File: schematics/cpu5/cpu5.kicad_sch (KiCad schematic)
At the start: 9 parts, among them J1 Conn_01x12, U1 74LS161, U2 74LS161, U3 74LS573, U4 74LS04, U5 74LS08, U6 74LS32, U7 74LS08

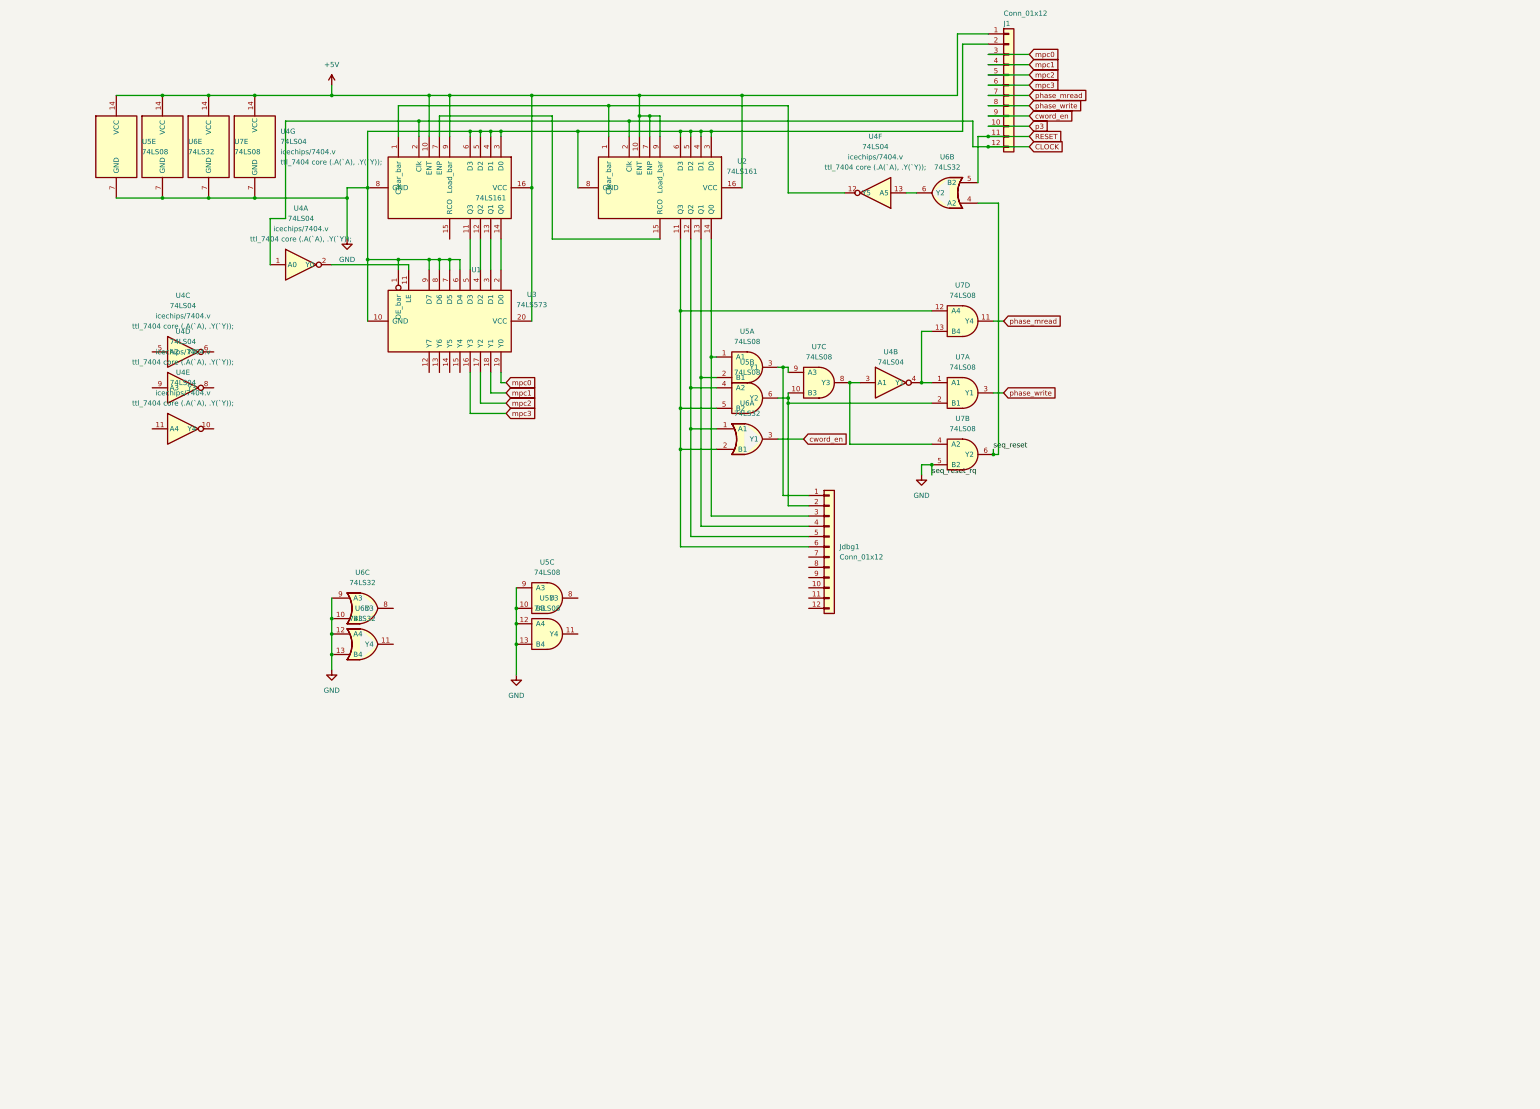
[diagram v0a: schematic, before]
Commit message: microcode rom works
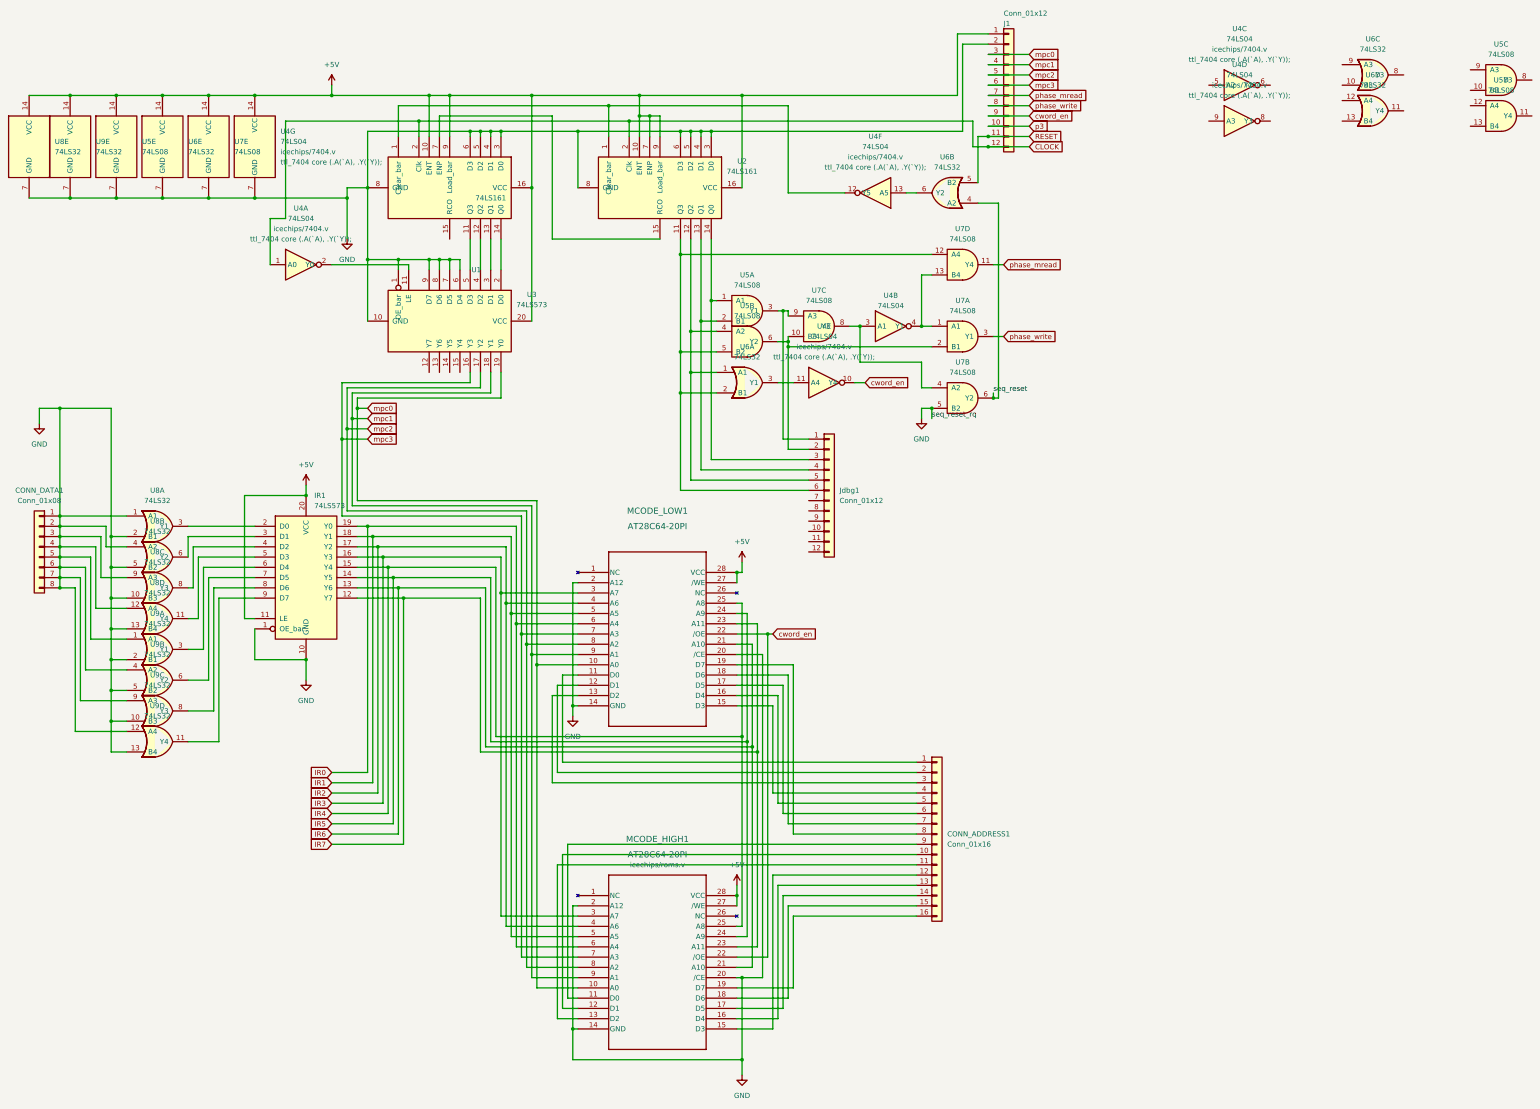
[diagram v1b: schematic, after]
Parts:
- added CONN_ADDRESS1: Conn_01x16, Connector_PinHeader_2.54mm:PinHeader_1x16_P2.54mm_Vertical, symbol Connector_Generic:Conn_01x16
- added CONN_DATA1: Conn_01x08, Connector_PinHeader_2.54mm:PinHeader_1x08_P2.54mm_Vertical, symbol Connector_Generic:Conn_01x08
- added IR1: 74LS573, Package_DIP:DIP-20_W7.62mm, symbol 7400_ice:74LS573
- added MCODE_HIGH1, MCODE_LOW1: AT28C64-20PI, Package_DIP:DIP-28_W15.24mm, symbol at28c64:AT28C64-20PI
- added U8, U9: 74LS32, Package_DIP:DIP-14_W7.62mm, symbol 7400_ice:74LS32
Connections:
- net +5V: now also IR1.11 (LE), IR1.20 (VCC), MCODE_HIGH1.27 (/WE), MCODE_HIGH1.28 (VCC), MCODE_LOW1.27 (/WE), MCODE_LOW1.28 (VCC), U8.14 (VCC), U9.14 (VCC)
- net GND: now also CONN_DATA1.1 (Pin_1), CONN_DATA1.2 (Pin_2), CONN_DATA1.3 (Pin_3), CONN_DATA1.4 (Pin_4), CONN_DATA1.5 (Pin_5), CONN_DATA1.6 (Pin_6), CONN_DATA1.7 (Pin_7), CONN_DATA1.8 (Pin_8), IR1.1 (OE_bar), IR1.10 (GND), MCODE_HIGH1.14 (GND), MCODE_HIGH1.2 (A12), MCODE_HIGH1.20 (/CE), MCODE_LOW1.14 (GND), MCODE_LOW1.2 (A12), MCODE_LOW1.20 (/CE), U8.1 (A1), U8.10 (B3), U8.12 (A4), U8.13 (B4), U8.2 (B1), U8.4 (A2), U8.5 (B2), U8.7 (GND), U8.9 (A3), U9.1 (A1), U9.10 (B3), U9.12 (A4), U9.13 (B4), U9.2 (B1), U9.4 (A2), U9.5 (B2), U9.7 (GND), U9.9 (A3); no longer U5.10 (B3), U5.12 (A4), U5.13 (B4), U5.9 (A3), U6.10 (B3), U6.12 (A4), U6.13 (B4), U6.9 (A3)
- net cword_en: now also U4.10 (Y4), MCODE_HIGH1.22 (/OE), MCODE_LOW1.22 (/OE); no longer U6.3 (Y1)
- net mpc0: now also MCODE_HIGH1.10 (A0), MCODE_LOW1.10 (A0)
- net mpc1: now also MCODE_HIGH1.9 (A1), MCODE_LOW1.9 (A1)
- net mpc2: now also MCODE_HIGH1.8 (A2), MCODE_LOW1.8 (A2)
- net mpc3: now also MCODE_HIGH1.7 (A3), MCODE_LOW1.7 (A3)
- net at U4.11 (A4): now also U6.3 (Y1)
- new net: IR1.7 (D5), U9.6 (Y2)
- new net: IR1.9 (D7), U9.11 (Y4)
- new net: IR1.2 (D0), U8.3 (Y1)
- new net: IR1.4 (D2), U8.8 (Y3)
- new net: IR1.5 (D3), U8.11 (Y4)
- new net: CONN_ADDRESS1.1 (Pin_1), MCODE_LOW1.11 (D0)
- new net: CONN_ADDRESS1.10 (Pin_10), MCODE_HIGH1.12 (D1)
- new net: CONN_ADDRESS1.11 (Pin_11), MCODE_HIGH1.13 (D2)
- new net: CONN_ADDRESS1.12 (Pin_12), MCODE_HIGH1.15 (D3)
- new net: CONN_ADDRESS1.13 (Pin_13), MCODE_HIGH1.16 (D4)
- new net: CONN_ADDRESS1.14 (Pin_14), MCODE_HIGH1.17 (D5)
- new net: CONN_ADDRESS1.15 (Pin_15), MCODE_HIGH1.18 (D6)
- new net: CONN_ADDRESS1.16 (Pin_16), MCODE_HIGH1.19 (D7)
- new net: CONN_ADDRESS1.2 (Pin_2), MCODE_LOW1.12 (D1)
- new net: CONN_ADDRESS1.3 (Pin_3), MCODE_LOW1.13 (D2)
- new net: CONN_ADDRESS1.4 (Pin_4), MCODE_LOW1.15 (D3)
- new net: CONN_ADDRESS1.5 (Pin_5), MCODE_LOW1.16 (D4)
- new net: CONN_ADDRESS1.6 (Pin_6), MCODE_LOW1.17 (D5)
- new net: CONN_ADDRESS1.7 (Pin_7), MCODE_LOW1.18 (D6)
- new net: CONN_ADDRESS1.8 (Pin_8), MCODE_LOW1.19 (D7)
- new net: CONN_ADDRESS1.9 (Pin_9), MCODE_HIGH1.11 (D0)
- new net: IR1.6 (D4), U9.3 (Y1)
- new net: IR1.3 (D1), U8.6 (Y2)
- new net: IR1.8 (D6), U9.8 (Y3)
- new net IR0: IR1.19 (Y0), MCODE_HIGH1.6 (A4), MCODE_LOW1.6 (A4)
- new net IR1: IR1.18 (Y1), MCODE_HIGH1.5 (A5), MCODE_LOW1.5 (A5)
- new net IR2: IR1.17 (Y2), MCODE_HIGH1.4 (A6), MCODE_LOW1.4 (A6)
- new net IR3: IR1.16 (Y3), MCODE_HIGH1.3 (A7), MCODE_LOW1.3 (A7)
- new net IR4: IR1.15 (Y4), MCODE_HIGH1.25 (A8), MCODE_LOW1.25 (A8)
- new net IR5: IR1.14 (Y5), MCODE_HIGH1.24 (A9), MCODE_LOW1.24 (A9)
- new net IR6: IR1.13 (Y6), MCODE_HIGH1.21 (A10), MCODE_LOW1.21 (A10)
- new net IR7: IR1.12 (Y7), MCODE_HIGH1.23 (A11), MCODE_LOW1.23 (A11)
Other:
- moved on the sheet: Jdbg1, U4B, U4C, U4D, U4E, U5A, U5B, U5C, U5D, U6A, U6C, U6D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

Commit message: nop works
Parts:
- removed IR1, U3: 74LS573, Package_DIP:DIP-20_W7.62mm, symbol 7400_ice:74LS573
- added IR1, U10, U11: 74LS574, Package_DIP:DIP-20_W7.62mm, symbol 7400_ice:74LS574
- added J2: Conn_01x03, Connector_PinHeader_2.54mm:PinHeader_1x03_P2.54mm_Vertical, symbol Connector_Generic:Conn_01x03
- added J3: Conn_01x40, Connector_PinHeader_2.54mm:PinHeader_1x40_P2.54mm_Vertical, symbol Connector_Generic:Conn_01x40
- added JFlags1: Conn_01x04, Connector_PinHeader_1.00mm:PinHeader_1x04_P1.00mm_Vertical, symbol Connector_Generic:Conn_01x04
- added U12, U21, U26, U31: 74LS08, Package_DIP:DIP-14_W7.62mm, symbol 7400_ice:74LS08
- added U13, U14, U15, U16, U17, U18, U19, U20, U27: 74LS138, Package_DIP:DIP-16_W7.62mm, symbol 7400_ice:74LS138
- added U22, U28: 74LS04, Package_DIP:DIP-14_W7.62mm, symbol 7400_ice:74LS04
- added U23, U25: 74LS86, Package_DIP:DIP-14_W7.62mm, symbol 7400_ice:74LS86
- added U24, U29, U30, U32, U33: 74LS32, Package_DIP:DIP-14_W7.62mm, symbol 7400_ice:74LS32
- added U34: 74LS74, Package_DIP:DIP-14_W7.62mm, symbol 7400_ice:74LS74
- added U35, U36, U42: 74LS541, Package_DIP:DIP-20_W7.62mm, symbol 7400_ice:74LS541
- CONN_DATA1: VerilogModulePort (none) -> 1,2,3,4,5,6,7,8
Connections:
- net +5V: now also IR1.20 (VCC), U10.20 (VCC), U11.20 (VCC), U12.14 (VCC), U13.16 (VCC), U14.16 (VCC), U15.16 (VCC), U16.16 (VCC), U17.16 (VCC), U18.16 (VCC), U19.16 (VCC), U20.16 (VCC), U21.14 (VCC), U22.14 (VCC), U23.14 (VCC), U24.14 (VCC), U25.14 (VCC), U26.14 (VCC), U27.16 (VCC), U27.6 (Enable3), U28.14 (VCC), U29.14 (VCC), U30.14 (VCC), U31.14 (VCC), U32.14 (VCC), U33.14 (VCC), U34.14 (VCC), U34.4 (nS1), U35.20 (VCC), U35.8 (A6), U35.9 (A7), U36.20 (VCC), U36.4 (A2), U36.5 (A3), U36.6 (A4), U36.7 (A5), U36.9 (A7), U42.2 (A0), U42.20 (VCC), U42.3 (A1), U42.4 (A2), U42.5 (A3), U42.6 (A4), U42.7 (A5), U42.8 (A6), U42.9 (A7); no longer U1.9 (Load_bar), U2.9 (Load_bar)
- net CLOCK: now also U26.13 (B4); no longer U4.1 (A0)
- net GND: now also MCODE_HIGH1.22 (/OE), MCODE_LOW1.22 (/OE), IR1.1 (OE_bar), IR1.10 (GND), U10.1 (OE_bar), U10.10 (GND), U11.1 (OE_bar), U11.10 (GND), U12.7 (GND), U13.4 (Enable1_bar), U13.8 (GND), U14.4 (Enable1_bar), U14.8 (GND), U15.4 (Enable1_bar), U15.8 (GND), U16.4 (Enable1_bar), U16.8 (GND), U17.4 (Enable1_bar), U17.8 (GND), U18.4 (Enable1_bar), U18.8 (GND), U19.4 (Enable1_bar), U19.8 (GND), U20.4 (Enable1_bar), U20.8 (GND), U21.7 (GND), U22.7 (GND), U23.7 (GND), U24.7 (GND), U25.7 (GND), U26.7 (GND), U27.4 (Enable1_bar), U27.5 (Enable2_bar), U27.8 (GND), U28.7 (GND), U29.7 (GND), U30.7 (GND), U31.7 (GND), U32.7 (GND), U33.7 (GND), U34.7 (GND), U35.1 (OE1_bar), U35.10 (GND), U35.7 (A5), U36.1 (OE1_bar), U36.10 (GND), U36.8 (A6), U42.10 (GND), U42.19 (OE2_bar); no longer CONN_DATA1.1 (Pin_1), CONN_DATA1.2 (Pin_2), CONN_DATA1.3 (Pin_3), CONN_DATA1.4 (Pin_4), CONN_DATA1.5 (Pin_5), CONN_DATA1.6 (Pin_6), CONN_DATA1.7 (Pin_7), CONN_DATA1.8 (Pin_8), U7.5 (B2), U8.1 (A1), U8.12 (A4), U8.4 (A2), U8.9 (A3), U9.1 (A1), U9.12 (A4), U9.4 (A2), U9.9 (A3)
- net IR0: now also IR1.19 (Y0), U27.1 (A0), U35.2 (A0)
- net IR1: now also IR1.18 (Y1), U27.2 (A1), U35.3 (A1)
- net IR2: now also IR1.17 (Y2), U27.3 (A2), U35.4 (A2)
- net IR3: now also IR1.16 (Y3), U23.12 (A4), U23.4 (A2), U23.9 (A3), U25.1 (A1), U25.4 (A2), U35.5 (A3)
- net IR4: now also IR1.15 (Y4), U35.6 (A4)
- net IR5: now also IR1.14 (Y5)
- net IR6: now also IR1.13 (Y6)
- net IR7: now also IR1.12 (Y7)
- net RESET: now also U1.1 (Clear_bar), U2.1 (Clear_bar), U28.3 (A1), U34.1 (nR1); no longer U6.5 (B2)
- net cword_en: now also U5.8 (Y3), U10.11 (CLK), U11.11 (CLK); no longer MCODE_HIGH1.22 (/OE), MCODE_LOW1.22 (/OE), U4.10 (Y4)
- net mpc0: now also U1.14 (Q0)
- net mpc1: now also U1.13 (Q1)
- net mpc2: now also U1.12 (Q2)
- net mpc3: now also U1.11 (Q3)
- net phase_mread: now also U21.5 (B2)
- net phase_write: now also U12.10 (B3), U12.13 (B4), U12.2 (B1), U12.5 (B2), U21.10 (B3), U21.2 (B1)
- net seq_reset: now also U4.13 (A5), U24.12 (A4); no longer U6.4 (A2)
- net at Jdbg1.3 (Pin_3), U2.14 (Q0), U5.1 (A1): now also U5.9 (A3)
- net at Jdbg1.5 (Pin_5), U2.12 (Q2), U5.4 (A2): now also U5.10 (B3); no longer U6.1 (A1)
- net at Jdbg1.6 (Pin_6), U2.11 (Q3), U5.5 (B2)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: no longer U6.2 (B1)
- net iIR5: now reaches U9.6 (Y2)
- net iIR5: now also IR1.7 (D5)
- net at U4.11 (A4): now also U33.11 (Y4); no longer U6.3 (Y1)
- net iIR7: now reaches U9.11 (Y4)
- net iIR7: now also IR1.9 (D7)
- net iIR0: now reaches U8.3 (Y1)
- net iIR0: now also IR1.2 (D0)
- net iIR2: now reaches U8.8 (Y3)
- net iIR2: now also IR1.4 (D2)
- net at U5.11 (Y4): now also U26.4 (A2)
- net at U5.12 (A4): now also U6.6 (Y2)
- net at U5.13 (B4): now also U6.3 (Y1)
- net iIR3: now reaches U8.11 (Y4)
- net iIR3: now also IR1.5 (D3)
- net at U6.10 (B3): now also U23.11 (Y4)
- net at U6.8 (Y3): now also U21.12 (A4)
- net at U6.9 (A3): now also U27.13 (Y2)
- net at U6.11 (Y4): now also U21.13 (B4)
- net at U6.12 (A4): now also U27.12 (Y3)
- net at U6.13 (B4): now also U25.3 (Y1)
- net at CONN_ADDRESS1.1 (Pin_1): now also U35.18 (Y0), U36.18 (Y0); no longer MCODE_LOW1.11 (D0)
- net at CONN_ADDRESS1.10 (Pin_10): now also U42.17 (Y1); no longer MCODE_HIGH1.12 (D1)
- net at CONN_ADDRESS1.11 (Pin_11): now also U42.16 (Y2); no longer MCODE_HIGH1.13 (D2)
- net at CONN_ADDRESS1.12 (Pin_12): now also U42.15 (Y3); no longer MCODE_HIGH1.15 (D3)
- net at CONN_ADDRESS1.13 (Pin_13): now also U42.14 (Y4); no longer MCODE_HIGH1.16 (D4)
- net at CONN_ADDRESS1.14 (Pin_14): now also U42.13 (Y5); no longer MCODE_HIGH1.17 (D5)
- net at CONN_ADDRESS1.15 (Pin_15): now also U42.12 (Y6); no longer MCODE_HIGH1.18 (D6)
- net at CONN_ADDRESS1.16 (Pin_16): now also U42.11 (Y7); no longer MCODE_HIGH1.19 (D7)
- net at CONN_ADDRESS1.2 (Pin_2): now also U35.17 (Y1), U36.17 (Y1); no longer MCODE_LOW1.12 (D1)
- net at CONN_ADDRESS1.3 (Pin_3): now also U35.16 (Y2), U36.16 (Y2); no longer MCODE_LOW1.13 (D2)
- net at CONN_ADDRESS1.4 (Pin_4): now also U35.15 (Y3), U36.15 (Y3); no longer MCODE_LOW1.15 (D3)
- net at CONN_ADDRESS1.5 (Pin_5): now also U35.14 (Y4), U36.14 (Y4); no longer MCODE_LOW1.16 (D4)
- net at CONN_ADDRESS1.6 (Pin_6): now also U35.13 (Y5), U36.13 (Y5); no longer MCODE_LOW1.17 (D5)
- net at CONN_ADDRESS1.7 (Pin_7): now also U35.12 (Y6), U36.12 (Y6); no longer MCODE_LOW1.18 (D6)
- net at CONN_ADDRESS1.8 (Pin_8): now also U35.11 (Y7), U36.11 (Y7); no longer MCODE_LOW1.19 (D7)
- net at CONN_ADDRESS1.9 (Pin_9): now also U42.18 (Y0); no longer MCODE_HIGH1.11 (D0)
- net iIR4: now reaches U9.3 (Y1)
- net iIR4: now also IR1.6 (D4)
- net at U4.5 (A2): now also U13.10 (Y5)
- net at U4.6 (Y2): now also U24.13 (B4)
- net at U4.8 (Y3): now also U17.5 (Enable2_bar), U18.5 (Enable2_bar), U19.5 (Enable2_bar), U20.5 (Enable2_bar)
- net dbg_mcode15: now reaches U4.9 (A3)
- net dbg_mcode15: now also U11.12 (Y7), U13.5 (Enable2_bar), U14.5 (Enable2_bar), U15.5 (Enable2_bar), U16.5 (Enable2_bar)
- net iIR1: now reaches U8.6 (Y2)
- net iIR1: now also IR1.3 (D1)
- net iIR6: now reaches U9.8 (Y3)
- net iIR6: now also IR1.8 (D6)
- new net: U12.11 (Y4), U20.6 (Enable3)
- new net: U15.15 (Y0), U22.5 (A2)
- new net: U12.6 (Y2), U16.6 (Enable3)
- new net: U21.6 (Y2), U22.11 (A4)
- new net: U30.8 (Y3), U31.2 (B1)
- new net: U14.7 (Y7), U30.9 (A3), U33.4 (A2)
- new net: U21.8 (Y3), U22.13 (A5)
- new net: U34.3 (Clk1), U4.10 (Y4)
- new net: U16.12 (Y3), U22.1 (A0)
- new net: U13.7 (Y7), U29.4 (A2), U32.1 (A1)
- new net: U27.14 (Y1), U6.1 (A1)
- new net: U23.8 (Y3), U6.2 (B1)
- new net: MCODE_HIGH1.11 (D0), U11.2 (D0)
- new net: MCODE_HIGH1.12 (D1), U11.3 (D1)
- new net: MCODE_HIGH1.13 (D2), U11.4 (D2)
- new net: MCODE_HIGH1.15 (D3), U11.5 (D3)
- new net: MCODE_HIGH1.16 (D4), U11.6 (D4)
- new net: MCODE_HIGH1.17 (D5), U11.7 (D5)
- new net: MCODE_HIGH1.18 (D6), U11.8 (D6)
- new net: MCODE_HIGH1.19 (D7), U11.9 (D7)
- new net: U15.9 (Y6), U29.9 (A3), U32.4 (A2)
- new net: U16.9 (Y6), U30.1 (A1), U32.12 (A4)
- new net: U1.9 (Load_bar), U2.9 (Load_bar), U4.12 (Y5)
- new net: U16.15 (Y0), U28.11 (A4)
- new net: U16.7 (Y7), U33.12 (A4)
- new net: U31.11 (Y4), U42.1 (OE1_bar)
- new net: U28.6 (Y2), U31.12 (A4), U36.19 (OE2_bar)
- new net: U23.6 (Y2), U6.5 (B2)
- new net: U29.10 (B3), U29.12 (A4), U29.2 (B1), U29.5 (B2), U30.2 (B1), U30.5 (B2), U33.5 (B2), U34.2 (D1), U34.6 (nQ1)
- new net: U26.12 (A4), U28.4 (Y1)
- new net: U23.13 (B4), U24.6 (Y2)
- new net: U12.3 (Y1), U15.6 (Enable3)
- new net: U23.3 (Y1), U24.4 (A2), U25.5 (B2)
- new net: U24.1 (A1), U27.11 (Y4)
- new net: U24.2 (B1), U25.6 (Y2)
- new net: U24.3 (Y1), U26.1 (A1)
- new net: U27.15 (Y0), U6.4 (A2)
- new net: U30.6 (Y2), U31.1 (A1)
- new net: U15.12 (Y3), U22.3 (A1)
- new net: U16.11 (Y4), U28.13 (A5)
- new net: IR1.11 (CLK), U32.8 (Y3)
- new net: MCODE_LOW1.11 (D0), U10.2 (D0)
- new net: MCODE_LOW1.12 (D1), U10.3 (D1)
- new net: MCODE_LOW1.13 (D2), U10.4 (D2)
- new net: MCODE_LOW1.15 (D3), U10.5 (D3)
- new net: MCODE_LOW1.16 (D4), U10.6 (D4)
- new net: MCODE_LOW1.17 (D5), U10.7 (D5)
- new net: MCODE_LOW1.18 (D6), U10.8 (D6)
- new net: MCODE_LOW1.19 (D7), U10.9 (D7)
- new net: U12.8 (Y3), U19.6 (Enable3)
- new net: U24.8 (Y3), U25.2 (B1)
- new net: U14.15 (Y0), U30.4 (A2), U33.1 (A1)
- new net: U15.7 (Y7), U29.13 (B4), U33.9 (A3)
- new net: U13.9 (Y6), U29.1 (A1), U30.12 (A4)
- new net: U26.10 (B3), U26.3 (Y1)
- new net: U26.6 (Y2), U26.9 (A3)
- new net: U21.11 (Y4), U26.5 (B2)
- new net: U26.2 (B1), U27.7 (Y7)
- new net: U31.4 (A2), U33.3 (Y1)
- new net: U31.5 (B2), U33.6 (Y2)
- new net ALUFd: J3.19 (Pin_19), U14.11 (Y4)
- new net ALUd: J3.21 (Pin_21), U14.13 (Y2)
- new net ALUlatch: J3.23 (Pin_23), U24.11 (Y4)
- new net Ai: J3.4 (Pin_4), U21.3 (Y1)
- new net Ao: J3.3 (Pin_3), U22.8 (Y3)
- new net Bi: J3.8 (Pin_8), U22.4 (Y1)
- new net Bo: J3.28 (Pin_28), U13.15 (Y0)
- new net Condition_bar: U26.8 (Y3), U33.13 (B4)
- new net DATA0: CONN_DATA1.1 (Pin_1), U8.1 (A1)
- new net DATA1: CONN_DATA1.2 (Pin_2), U8.4 (A2)
- new net DATA2: CONN_DATA1.3 (Pin_3), U8.9 (A3)
- new net DATA3: CONN_DATA1.4 (Pin_4), U8.12 (A4)
- new net DATA4: CONN_DATA1.5 (Pin_5), U9.1 (A1)
- new net DATA5: CONN_DATA1.6 (Pin_6), U9.4 (A2)
- new net DATA6: CONN_DATA1.7 (Pin_7), U9.9 (A3)
- new net DATA7: CONN_DATA1.8 (Pin_8), U9.12 (A4)
- new net DI_IVo: J2.2 (Pin_2), U28.8 (Y3)
- new net F_C: JFlags1.2 (Pin_2), U23.10 (B3), U24.10 (B3)
- new net F_OF: JFlags1.4 (Pin_4), U23.2 (B1)
- new net F_SF: JFlags1.3 (Pin_3), U23.1 (A1)
- new net F_Z: JFlags1.1 (Pin_1), U23.5 (B2), U24.5 (B2), U24.9 (A3)
- new net Fi: J3.6 (Pin_6), U28.12 (Y5)
- new net Fo: J3.18 (Pin_18), U14.10 (Y5)
- new net IRi: J3.7 (Pin_7), U28.10 (Y4), U32.9 (A3)
- new net MFa: J3.20 (Pin_20), U14.12 (Y3)
- new net MHi: J3.10 (Pin_10), U16.10 (Y5)
- new net MHo: J3.25 (Pin_25), U13.12 (Y3)
- new net MLi: J3.14 (Pin_14), U15.11 (Y4)
- new net MLo: J3.24 (Pin_24), U13.11 (Y4)
- new net MREAD: J3.2 (Pin_2), U22.10 (Y4)
- new net MWRITE: J3.1 (Pin_1), U22.12 (Y5)
- new net OFFi: J3.9 (Pin_9), U22.6 (Y2)
- new net SELa: J2.1 (Pin_1), U11.15 (Y4), U28.5 (A2)
- new net SELhigh: J2.3 (Pin_3), U11.13 (Y6)
- new net SHi: J3.16 (Pin_16), U15.14 (Y1)
- new net SHo: J3.27 (Pin_27), U13.14 (Y1)
- new net SLi: J3.15 (Pin_15), U15.13 (Y2)
- new net SLmm: J3.12 (Pin_12), U16.14 (Y1)
- new net SLo: J3.26 (Pin_26), U13.13 (Y2)
- new net SLpp: J3.11 (Pin_11), U16.13 (Y2)
- new net Sa: J3.22 (Pin_22), U14.14 (Y1)
- new net Srst: J3.5 (Pin_5), U22.2 (Y0)
- new net dbgB_as_PC: U30.10 (B3), U30.13 (B4), U32.13 (B4), U32.2 (B1), U32.5 (B2), U33.10 (B3), U33.2 (B1), U34.5 (Q1)
- new net dbg_mcode0: U10.19 (Y0), U13.1 (A0), U14.1 (A0), U15.1 (A0), U16.1 (A0), U17.1 (A0), U18.1 (A0), U19.1 (A0), U20.1 (A0), U36.2 (A0)
- new net dbg_mcode1: U10.18 (Y1), U13.2 (A1), U14.2 (A1), U15.2 (A1), U16.2 (A1), U17.2 (A1), U18.2 (A1), U19.2 (A1), U20.2 (A1), U36.3 (A1)
- new net dbg_mcode10: U11.17 (Y2), U21.4 (A2)
- new net dbg_mcode11: U11.16 (Y3), U21.9 (A3)
- new net dbg_mcode13: U11.14 (Y5), U28.9 (A3)
- new net dbg_mcode2: U10.17 (Y2), U13.3 (A2), U14.3 (A2), U15.3 (A2), U16.3 (A2), U17.3 (A2), U18.3 (A2), U19.3 (A2), U20.3 (A2)
- new net dbg_mcode3: U10.16 (Y3), U13.6 (Enable3), U17.6 (Enable3)
- new net dbg_mcode4: U10.15 (Y4), U14.6 (Enable3), U18.6 (Enable3)
- new net dbg_mcode5: U10.14 (Y5), U12.1 (A1), U12.9 (A3)
- new net dbg_mcode6: U10.13 (Y6), U12.12 (A4), U12.4 (A2)
- new net dbg_mcode7: U10.12 (Y7), U7.5 (B2)
- new net dbg_mcode8: U11.19 (Y0), U21.1 (A1)
- new net dbg_mcode9: U11.18 (Y1), U22.9 (A3)
- new net ei: J3.13 (Pin_13), U15.10 (Y5)
- new net init_ir: U26.11 (Y4), U32.10 (B3)
- new net outFFXX: J3.17 (Pin_17), U14.9 (Y6), U31.13 (B4), U35.19 (OE2_bar)
- new net pACa: J3.29 (Pin_29), U31.6 (Y2)
- new net pACpp: J3.31 (Pin_31), U32.11 (Y4)
- new net pAHi: J3.38 (Pin_38), U29.8 (Y3)
- new net pAHo: J3.40 (Pin_40), U29.3 (Y1)
- new net pALi: J3.37 (Pin_37), U29.11 (Y4)
- new net pALo: J3.39 (Pin_39), U29.6 (Y2)
- new net pBCa: J3.30 (Pin_30), U31.3 (Y1)
- new net pBCpp: J3.36 (Pin_36), U30.3 (Y1)
- new net pBHi: J3.33 (Pin_33), U32.6 (Y2)
- new net pBHo: J3.35 (Pin_35), U30.11 (Y4)
- new net pBLi: J3.32 (Pin_32), U33.8 (Y3)
- new net pBLo: J3.34 (Pin_34), U32.3 (Y1)
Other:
- moved on the sheet: U4A, U4C, U4D, U4E, U5C, U5D, U6A, U6B, U6C, U6D

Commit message: address marching with PC
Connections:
- net DATA0: no longer CONN_DATA1.1 (Pin_1), U8.1 (A1)
- net DATA1: no longer CONN_DATA1.2 (Pin_2), U8.4 (A2)
- net DATA2: no longer CONN_DATA1.3 (Pin_3), U8.9 (A3)
- net DATA3: no longer CONN_DATA1.4 (Pin_4), U8.12 (A4)
- net DATA4: no longer CONN_DATA1.5 (Pin_5), U9.1 (A1)
- net DATA5: no longer CONN_DATA1.6 (Pin_6), U9.4 (A2)
- net DATA6: no longer CONN_DATA1.7 (Pin_7), U9.9 (A3)
- net DATA7: no longer CONN_DATA1.8 (Pin_8), U9.12 (A4)
- net RESET_bar: now reaches U26.12 (A4), U28.4 (Y1)
- new net iDATA0: CONN_DATA1.1 (Pin_1), U8.1 (A1)
- new net iDATA1: CONN_DATA1.2 (Pin_2), U8.4 (A2)
- new net iDATA2: CONN_DATA1.3 (Pin_3), U8.9 (A3)
- new net iDATA3: CONN_DATA1.4 (Pin_4), U8.12 (A4)
- new net iDATA4: CONN_DATA1.5 (Pin_5), U9.1 (A1)
- new net iDATA5: CONN_DATA1.6 (Pin_6), U9.4 (A2)
- new net iDATA6: CONN_DATA1.7 (Pin_7), U9.9 (A3)
- new net iDATA7: CONN_DATA1.8 (Pin_8), U9.12 (A4)
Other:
- added sheet Registers (registers.kicad_sch)
